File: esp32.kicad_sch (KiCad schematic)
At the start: 47 parts, among them J2 Conn_01x05, SW1 Reset, SW2 BOOT, U6 ESP32-S3R8, U7 W25Q128JVSIQ, Y1 40MHz

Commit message: work in progress
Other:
- moved on the sheet: C39, U7

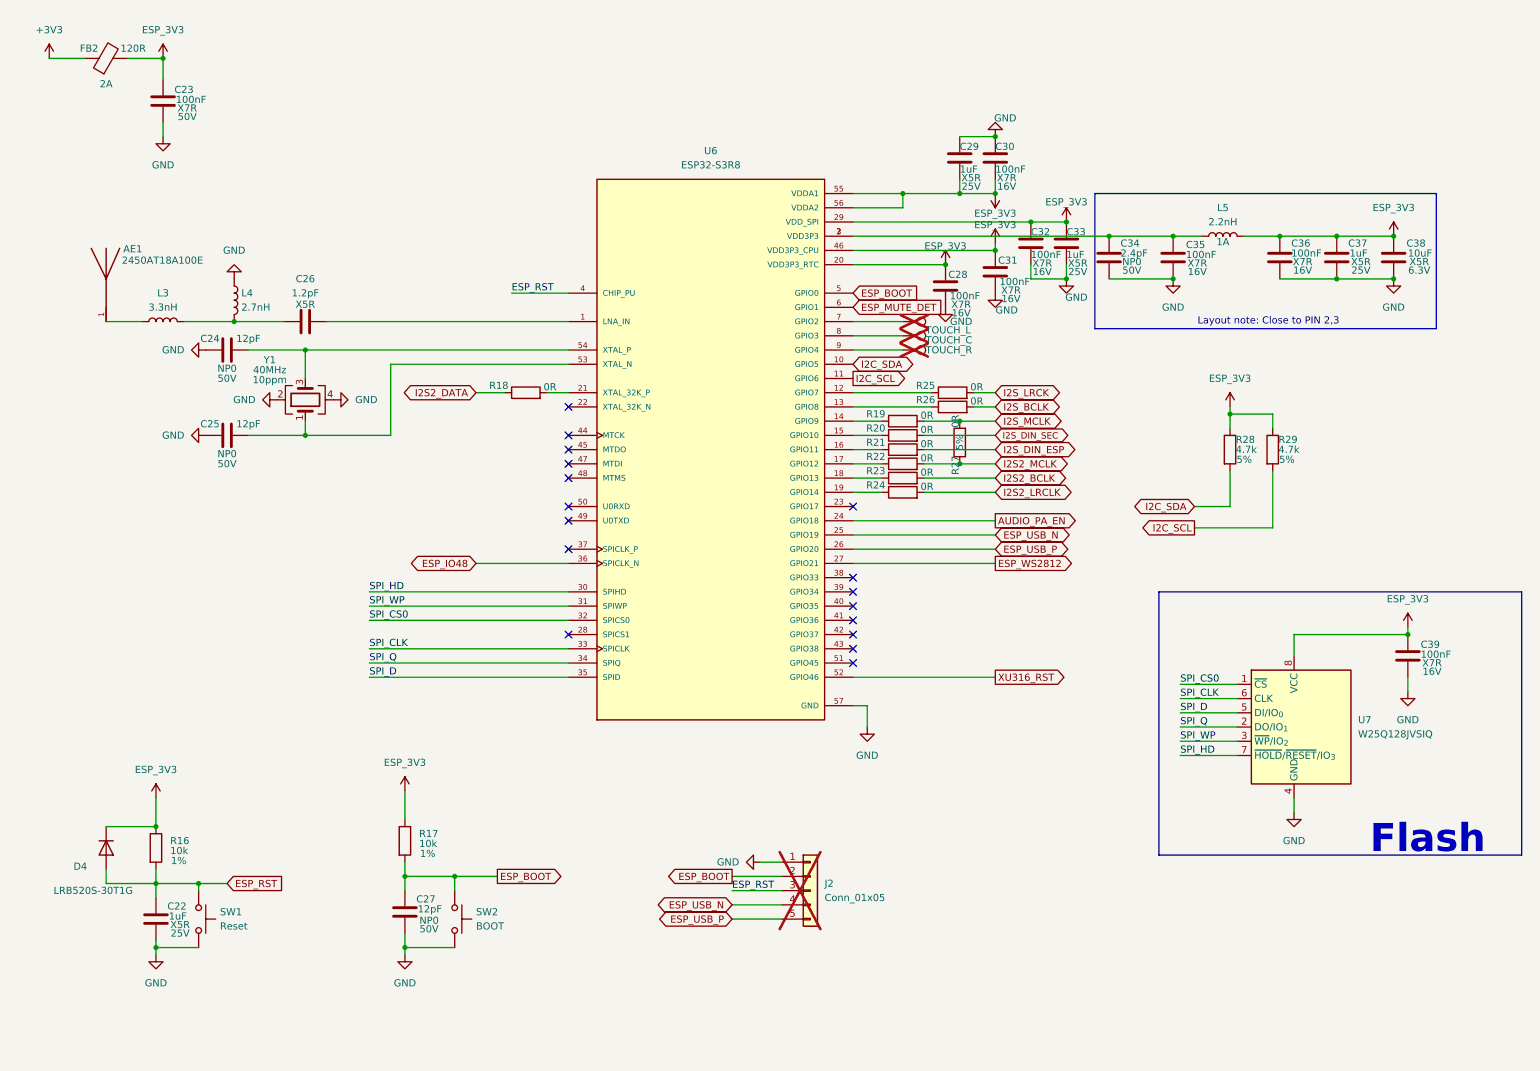
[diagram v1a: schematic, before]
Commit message: v2 hardware revision
MPR121 touch controller added to replace the esp32-s3 internal touch interface
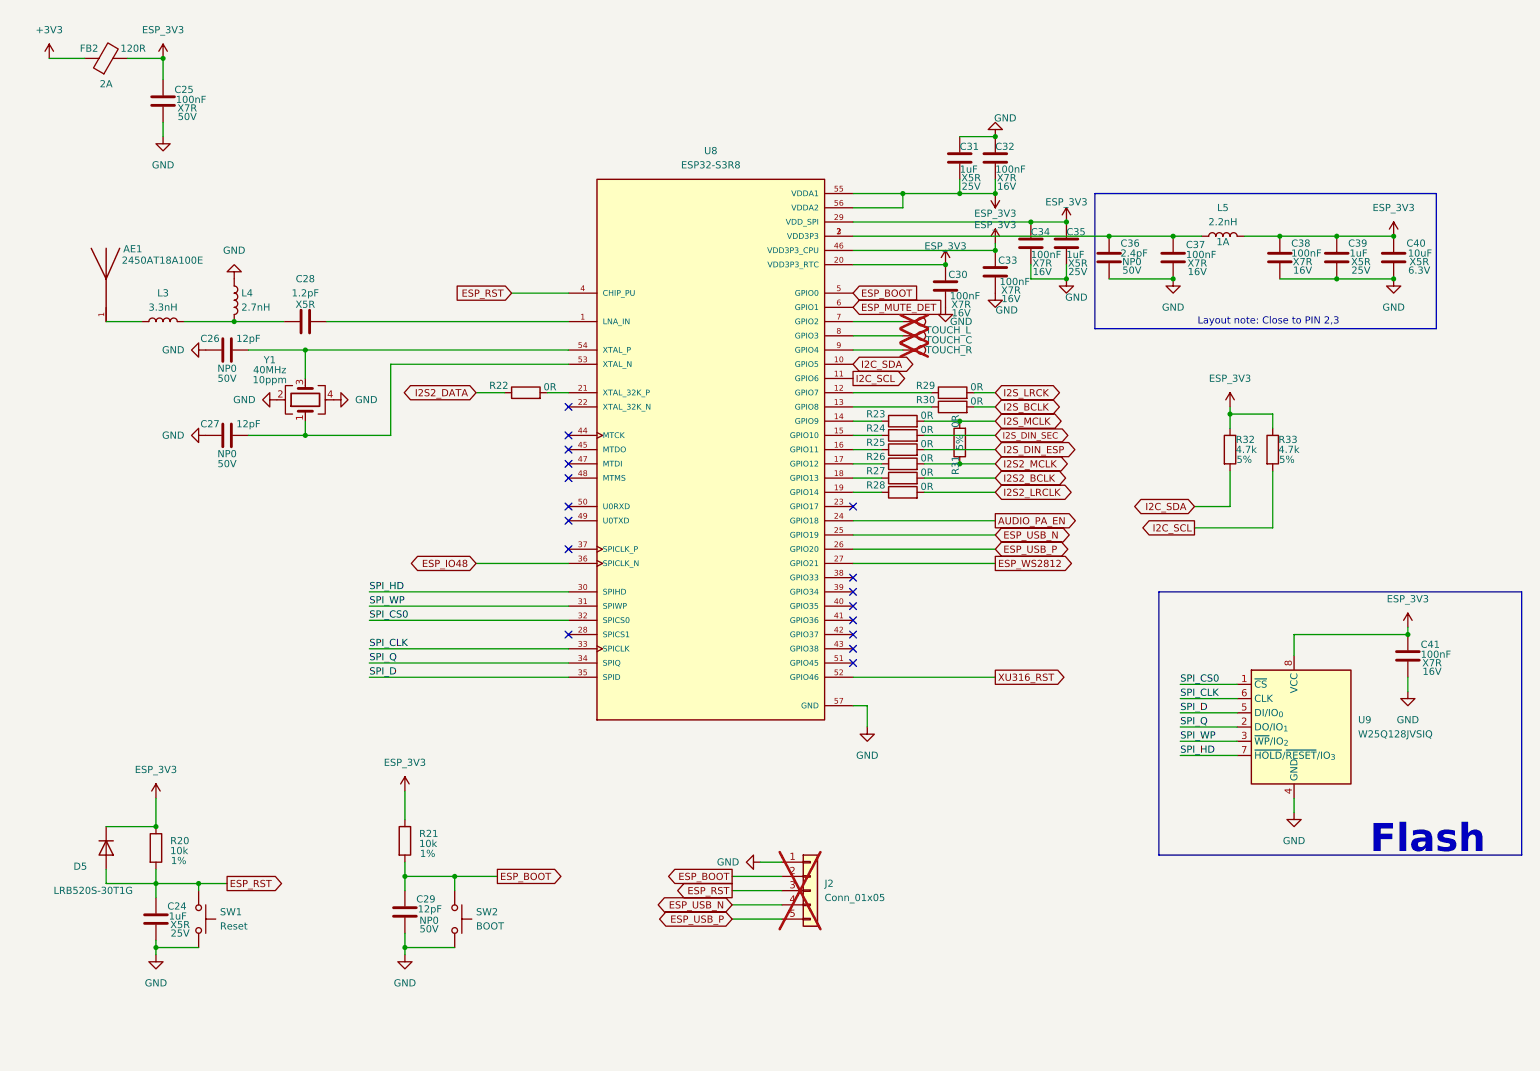
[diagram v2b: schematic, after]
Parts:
- renumbered C22 to C24, C23 to C25, C24 to C26, C25 to C27, C26 to C28, C27 to C29, C28 to C30, C29 to C31, C30 to C32, C31 to C33, C32 to C34, C33 to C35, C34 to C36, C35 to C37, C36 to C38, C37 to C39, C38 to C40, C39 to C41, D4 to D5, R16 to R20, R17 to R21, R18 to R22, R19 to R23, R20 to R24, R21 to R25, R22 to R26, R23 to R27, R24 to R28, R25 to R29, R26 to R30, R27 to R31, R28 to R32, R29 to R33, TP1 to TP7, TP2 to TP8, TP3 to TP9, U6 to U8, U7 to U9

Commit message: v2 hardware
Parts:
- removed TP7: TOUCH_L, TestPoint:TestPoint_Pad_2.5x2.5mm, symbol Connector:TestPoint
- removed TP8: TOUCH_C, TestPoint:TestPoint_Pad_2.5x2.5mm, symbol Connector:TestPoint
- removed TP9: TOUCH_R, TestPoint:TestPoint_Pad_2.5x2.5mm, symbol Connector:TestPoint
- added C98: 1uF, Capacitor_SMD:C_0402_1005Metric, symbol Device:C
- added C99: 100nF, Capacitor_SMD:C_0402_1005Metric, symbol Device:C
- added R72: 200k, Resistor_SMD:R_0402_1005Metric, symbol Device:R
- added R73: 1M, Resistor_SMD:R_0402_1005Metric, symbol Device:R
- added TP14: TOUCH_R, TestPoint:TestPoint_Pad_2.5x2.5mm, symbol Connector:TestPoint
- added TP15: TOUCH_C, TestPoint:TestPoint_Pad_2.5x2.5mm, symbol Connector:TestPoint
- added TP16: TOUCH_L, TestPoint:TestPoint_Pad_2.5x2.5mm, symbol Connector:TestPoint
- added U15: MPR121QR2, Onju:MPR121QR2, symbol New_Library:MPR121QR2
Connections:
- net +3V3: now also C99.1, U15.20 (VDD)
- net GND: now also C98.1, C99.2, R72.1, R73.2, U15.4 (ADDR), U15.6 (VSS)
- net I2C_SCL: now also U15.2 (SCL)
- net I2C_SDA: now also U15.3 (SDA)
- net XU316_RST: now also U8.23 (GPIO17); no longer U8.52 (GPIO46)
- net TOUCH_IRQ: now reaches U8.7 (GPIO2)
- net TOUCH_IRQ: now also U15.1 (~{IRQ})
- new net: C98.2, U15.5 (VREG)
- new net: TP15.1, U15.9 (ELEC1)
- new net: TP14.1, U15.10 (ELEC2)
- new net: R73.1, U15.11 (ELEC3), U15.12 (ELEC4), U15.13 (ELEC5), U15.14 (ELEC6), U15.15 (ELEC7), U15.16 (ELEC8), U15.17 (ELEC9), U15.18 (ELEC10), U15.19 (ELEC11)
- new net: R72.2, U15.7 (REXT)
- new net: TP16.1, U15.8 (ELEC0)
- no-connect marks 17 -> 19
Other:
- note added: "Touch"
- moved on the sheet: AE1, C24, C25, C26, C27, C28, C29, C30, C31, C32, C33, C34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
